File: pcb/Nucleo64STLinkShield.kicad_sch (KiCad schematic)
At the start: 6 parts, among them J1 SWD, J2 Debug, J3 UART, J4 USB Power, J5 Nucleo-64 ST-Link Selector

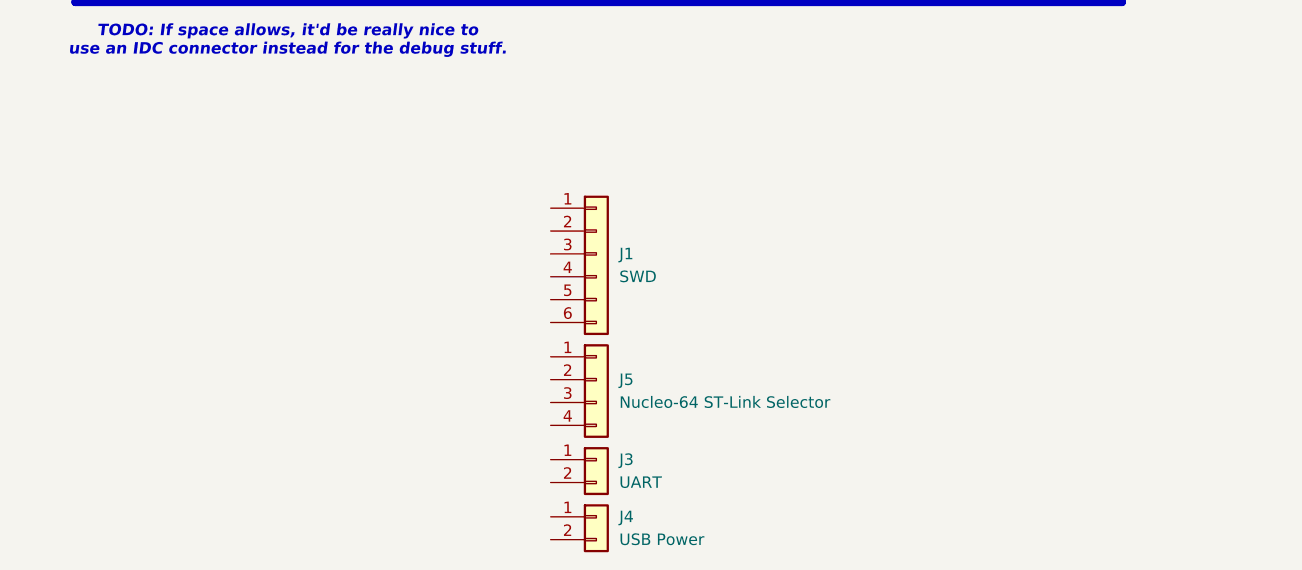
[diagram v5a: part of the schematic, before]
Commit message: Added nets for the pin sockets.
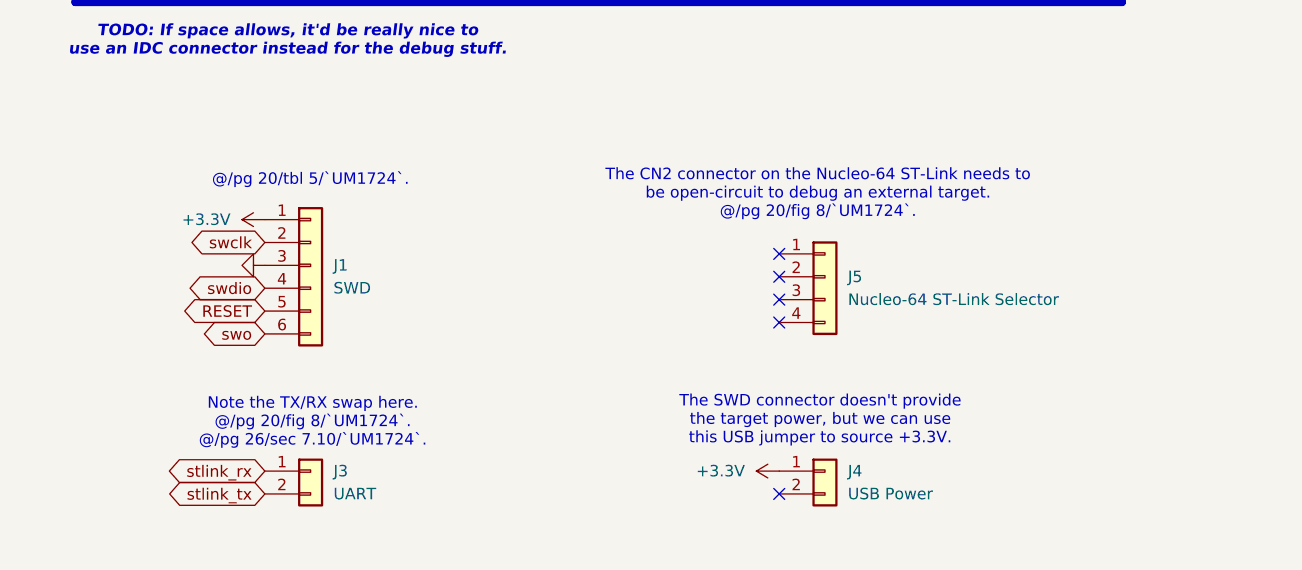
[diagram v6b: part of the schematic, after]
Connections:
- net +3.3V: now also J1.1 (Pin_1), J4.1 (Pin_1)
- net GND: now also J1.3 (Pin_3)
- net RESET: now also J1.5 (Pin_5)
- net stlink_rx: now also J3.1 (Pin_1)
- net stlink_tx: now also J3.2 (Pin_2)
- net swclk: now also J1.2 (Pin_2)
- net swdio: now also J1.4 (Pin_4)
- net swo: now also J1.6 (Pin_6)
- no-connect marks 0 -> 5
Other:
- note added: "@/pg 20/tbl 5/`UM1724`."
- note added: "Note the TX/RX swap here. @/pg 20/fig 8/`UM1724`. @/pg 26/sec 7.10/`UM1724`."
- note added: "The CN2 connector on the Nucleo-64 ST-Link needs to be open-circuit to debug an external target. @/pg 20/fig 8/`UM1724`."
- note added: "The SWD connector doesn't provide the target power, but we can use this USB jumper to source +3.3V."
- moved on the sheet: J1, J3, J4, J5

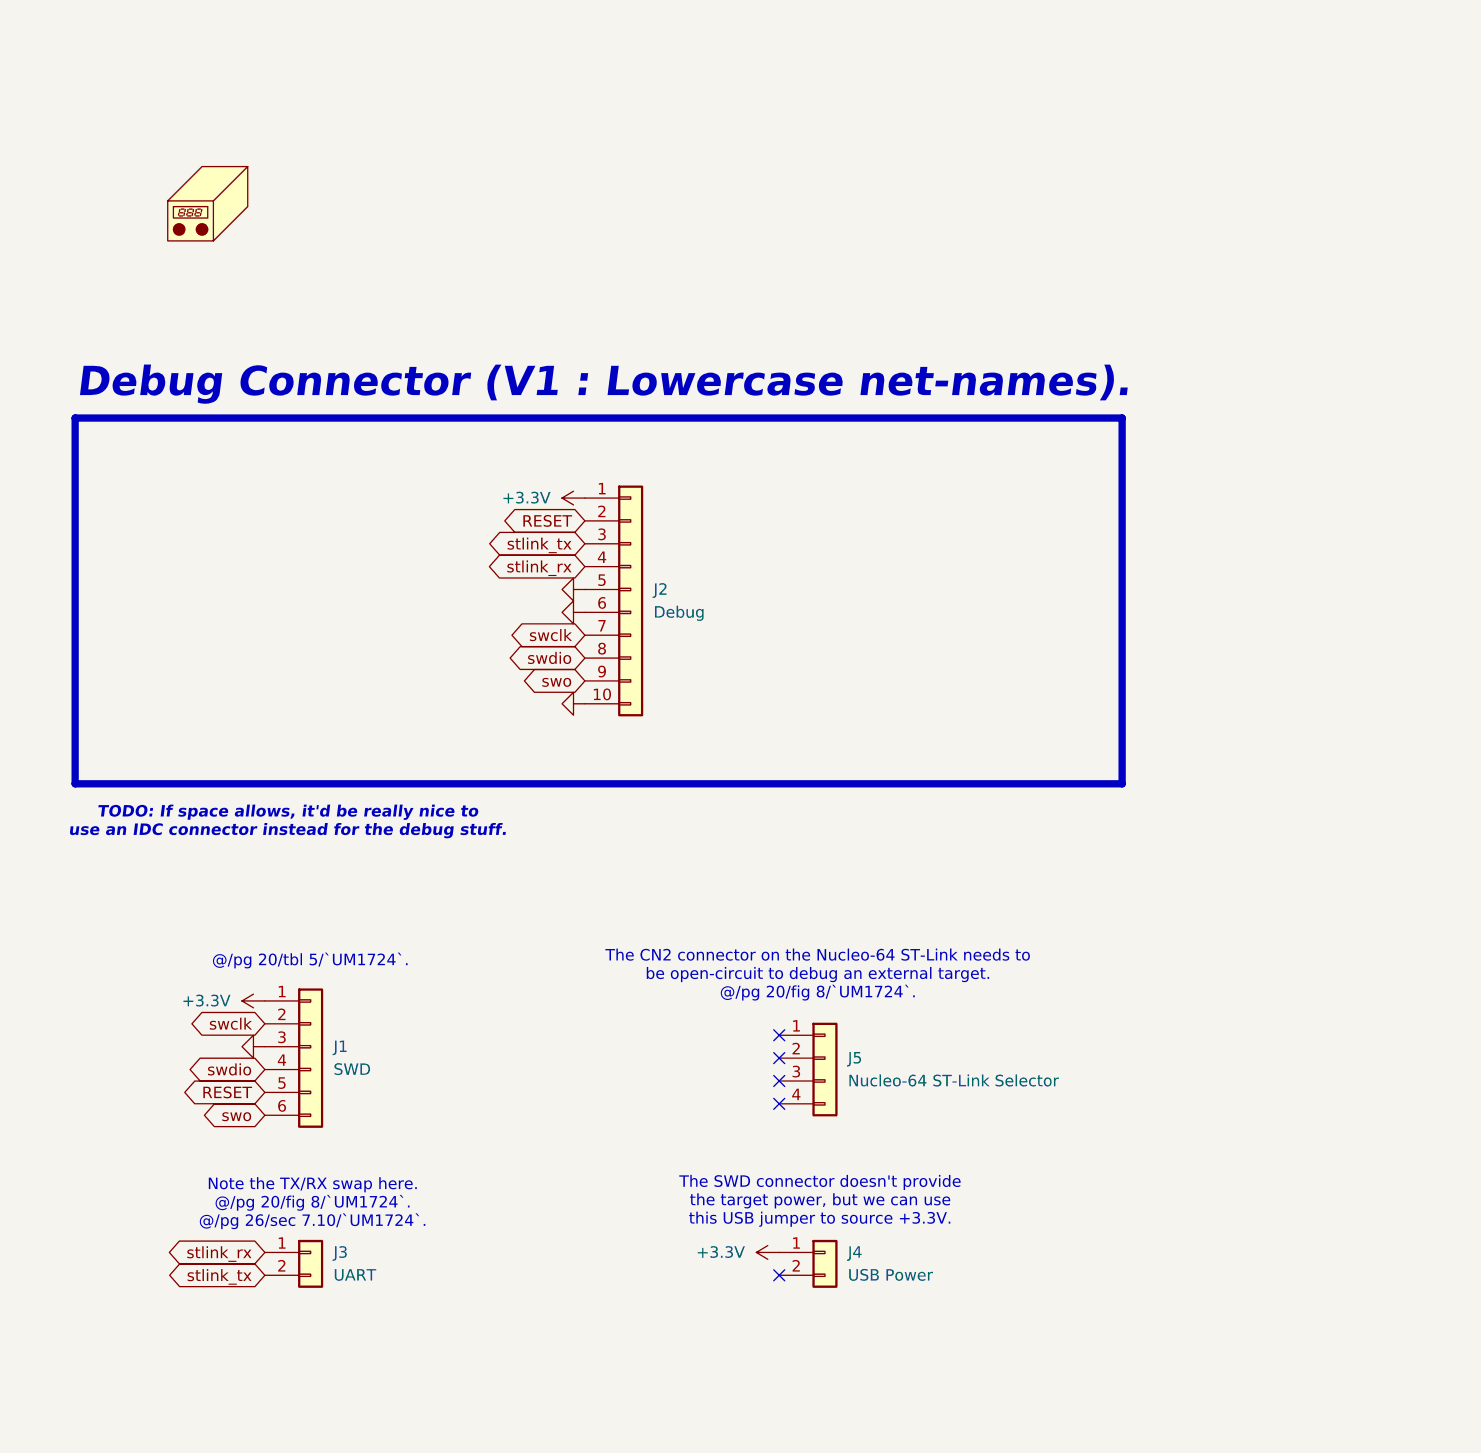
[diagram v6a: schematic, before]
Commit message: Added supporting components.
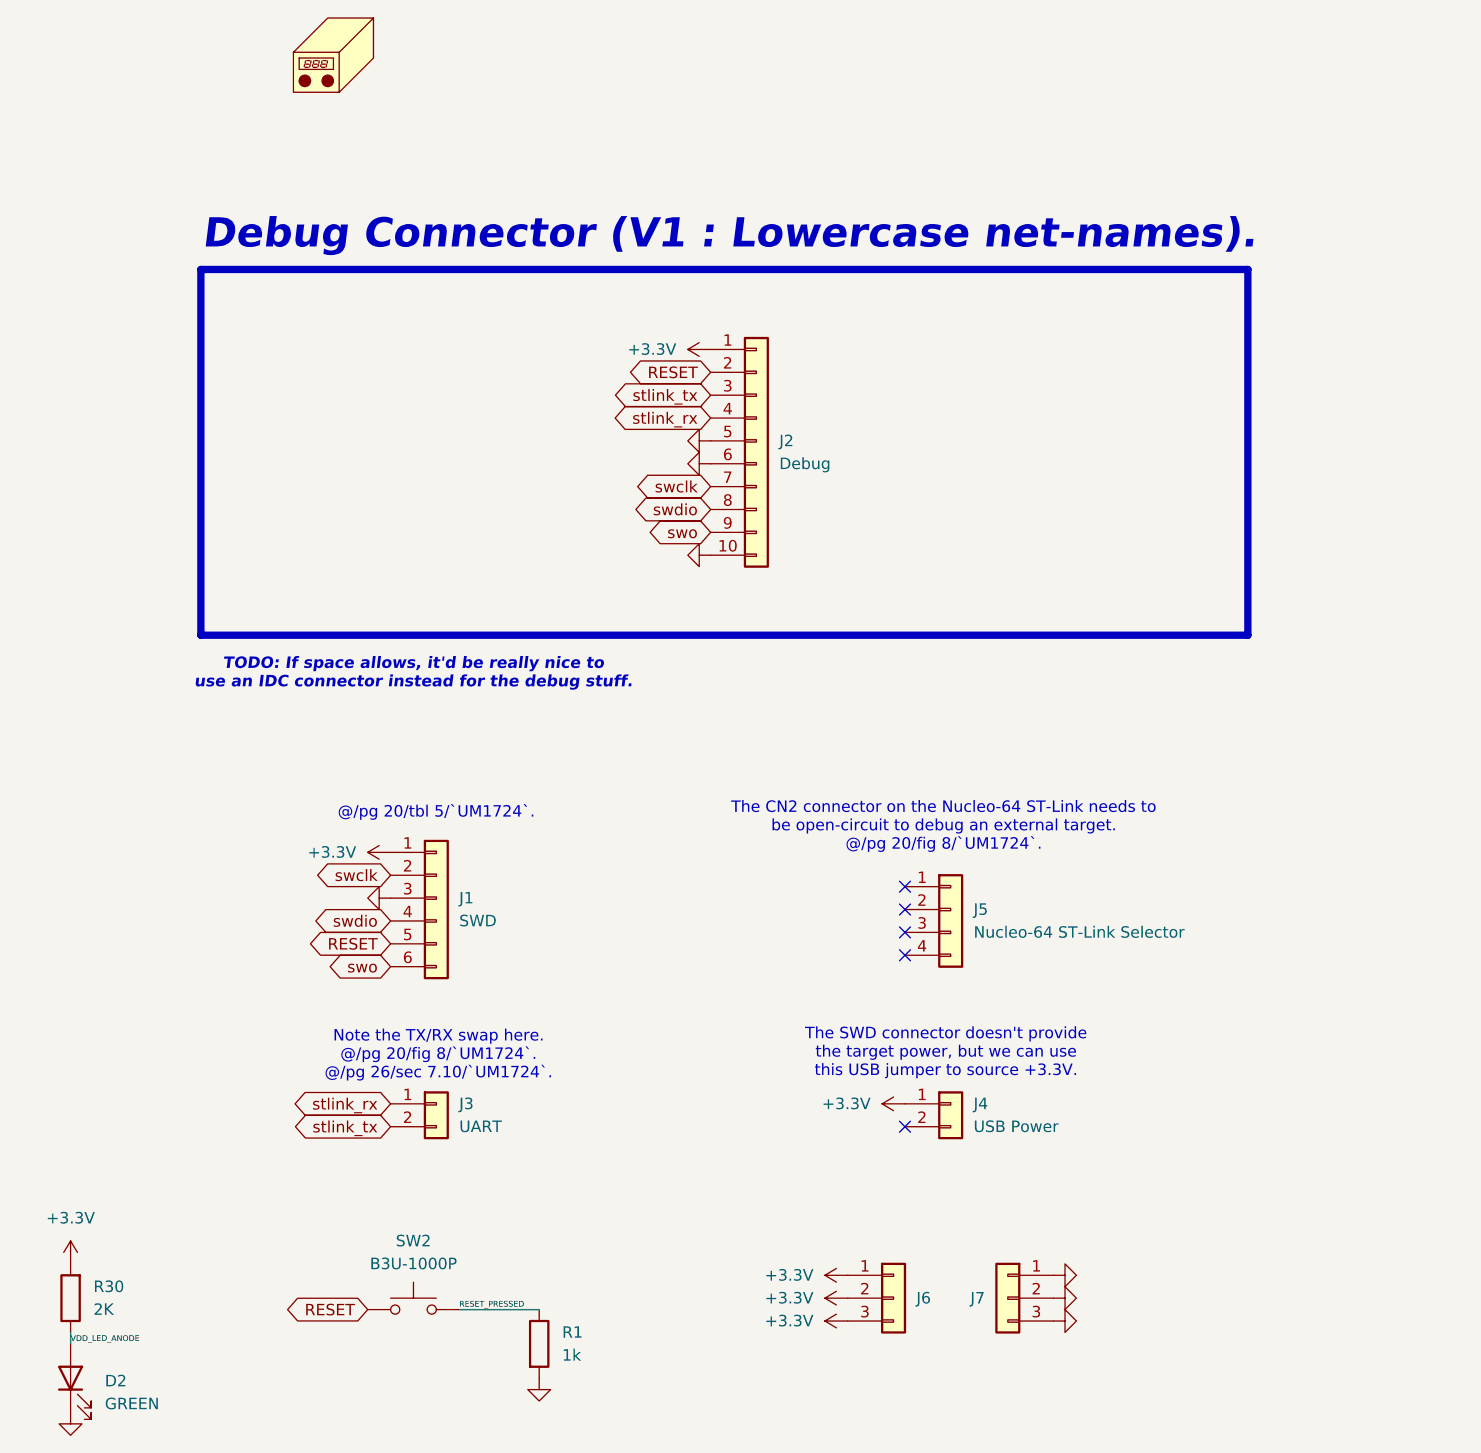
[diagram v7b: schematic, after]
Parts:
- added D2: GREEN, LED_SMD:LED_1206_3216Metric_Pad1.42x1.75mm_HandSolder, symbol Device:LED
- added J6, J7: Conn_01x06, Connector_PinHeader_2.54mm:PinHeader_1x03_P2.54mm_Vertical, symbol Connector_Generic:Conn_01x03
- added R1: 1k, Resistor_SMD:R_1206_3216Metric_Pad1.30x1.75mm_HandSolder, symbol Device:R
- added R30: 2K, Resistor_SMD:R_1206_3216Metric_Pad1.30x1.75mm_HandSolder, symbol Device:R
- added SW2: B3U-1000P, Button_Switch_SMD:SW_SPST_B3U-1000P, symbol Switch:SW_Push
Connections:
- net +3.3V: now also J6.1 (Pin_1), J6.2 (Pin_2), J6.3 (Pin_3), R30.2
- net GND: now also D2.1 (K), J7.1 (Pin_1), J7.2 (Pin_2), J7.3 (Pin_3), R1.2
- net RESET: now also SW2.2
- new net RESET_PRESSED: R1.1, SW2.1
- new net VDD_LED_ANODE: D2.2 (A), R30.1
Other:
- moved on the sheet: J1, J2, J3, J4, J5

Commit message: Routed the ST-Link shield.
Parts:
- J6, J7: value Conn_01x06 -> Conn_01x03
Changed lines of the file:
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@@
+	)
+	(symbol
+		(lib_id "power:GND")
+		(at 119.38 127 270)
+		(unit 1)
+		(exclude_from_sim no)
+		(in_bom yes)
+		(on_board yes)
+		(dnp no)
+		(fields_autoplaced yes)
+		(property "Reference" "#PWR02"
+			(at 113.03 127 0)
+			(effects
+				(font
+					(size 1.27 1.27)
+				)
+				(hide yes)
+			)
+		)
+		(property "Value" "GND"
+			(at 115.57 127.0001 90)
+			(effects
+				(font
+					(size 1.27 1.27)
+				)
+				(justify right)
+				(hide yes)
+			)
+		)
+		(property "Footprint" ""
+			(at 119.38 127 0)
+			(effects
+				(font
+					(size 1.27 1.27)
+				)
+				(hide yes)
+			)
+		)
+		(property "Datasheet" ""
+			(at 119.38 127 0)
+			(effects
+				(font
+					(size 1.27 1.27)
+				)
+				(hide yes)
+			)
+		)
+		(property "Description" "Power symbol creates a global label with name \"GND\" , ground"
+			(at 119.38 127 0)
+			(effects
+				(font
+					(size 1.27 1.27)
+				)
+				(hide yes)
+			)
+		)
+		(pin "1"
+		)
+		(instances
+			(project "Nucleo64STLinkShield"
+				(path "/dc931235-6a3d-461b-9fb0-f5879d72cf99"
+					(reference "#PWR02")
+					(unit 1)
+				)
+			)
+		)
 	)
 	(symbol
@@
 	)
 	(symbol
+		(lib_id "Connector_Generic:Conn_01x06")
+		(at 124.46 127 0)
+		(unit 1)
+		(exclude_from_sim no)
+		(in_bom yes)
+		(on_board yes)
+		(dnp no)
+		(property "Reference" "J1"
+			(at 127 127 0)
+			(effects
+				(font
+					(size 1.27 1.27)
+				)
+				(justify left)
+			)
+		)
+		(property "Value" "SWD"
+			(at 127 129.5399 0)
+			(effects
+				(font
+					(size 1.27 1.27)
+				)
+				(justify left)
+			)
+		)
+		(property "Footprint" "Connector_PinSocket_2.54mm:PinSocket_1x06_P2.54mm_Vertical"
+			(at 124.46 127 0)
+			(effects
+				(font
+					(size 1.27 1.27)
+				)
+				(hide yes)
+			)
+		)
+		(property "Datasheet" "~"
+			(at 124.46 127 0)
+			(effects
+				(font
+					(size 1.27 1.27)
+				)
+				(hide yes)
+			)
+		)
+		(property "Description" "Generic connector, single row, 01x06, script generated (kicad-library-utils/schlib/autogen/connector/)"
+			(at 124.46 127 0)
+			(effects
+				(font
+					(size 1.27 1.27)
+				)
+				(hide yes)
+			)
+		)
+		(pin "2"
+		)
+		(pin "1"
+		)
+		(pin "3"
+		)
+		(pin "5"
+		)
+		(pin "4"
+		)
+		(pin "6"
+		)
+		(instances
+			(project "Nucleo64STLinkShield"
+				(path "/dc931235-6a3d-461b-9fb0-f5879d72cf99"
+					(reference "J1")
+					(unit 1)
+				)
+			)
+		)
+	)
+	(symbol
 		(lib_id "power:GND")
 		(at 193.04 168.91 90)
@@
 	)
 	(symbol
-		(lib_id "power:GND")
-		(at 119.38 127 270)
-		(unit 1)
-		(exclude_from_sim no)
-		(in_bom yes)
-		(on_board yes)
-		(dnp no)
-		(fields_autoplaced yes)
-		(property "Reference" "#PWR02"
-			(at 113.03 127 0)
-			(effects
-				(font
-					(size 1.27 1.27)
-				)
-				(hide yes)
-			)
-		)
-		(property "Value" "GND"
-			(at 115.57 127.0001 90)
-			(effects
-				(font
-					(size 1.27 1.27)
-				)
-				(justify right)
-				(hide yes)
-			)
-		)
-		(property "Footprint" ""
-			(at 119.38 127 0)
-			(effects
-				(font
-					(size 1.27 1.27)
-				)
-				(hide yes)
-			)
-		)
-		(property "Datasheet" ""
-			(at 119.38 127 0)
-			(effects
-				(font
-					(size 1.27 1.27)
-				)
-				(hide yes)
-			)
-		)
-		(property "Description" "Power symbol creates a global label with name \"GND\" , ground"
-			(at 119.38 127 0)
-			(effects
-				(font
-					(size 1.27 1.27)
-				)
-				(hide yes)
-			)
-		)
-		(pin "1"
-		)
-		(instances
-			(project "Nucleo64STLinkShield"
-				(path "/dc931235-6a3d-461b-9fb0-f5879d72cf99"
-					(reference "#PWR02")
-					(unit 1)
-				)
-			)
-		)
-	)
-	(symbol
 		(lib_id "power:+3.3V")
 		(at 119.38 121.92 90)
@@
 				(path "/dc931235-6a3d-461b-9fb0-f5879d72cf99"
 					(reference "#PWR01")
-					(unit 1)
-				)
-			)
-		)
-	)
-	(symbol
-		(lib_id "Connector_Generic:Conn_01x06")
-		(at 124.46 127 0)
-		(unit 1)
-		(exclude_from_sim no)
-		(in_bom yes)
-		(on_board yes)
-		(dnp no)
-		(fields_autoplaced yes)
-		(property "Reference" "J1"
-			(at 127 126.9999 0)
-			(effects
-				(font
-					(size 1.27 1.27)
-				)
-				(justify left)
-			)
-		)
-		(property "Value" "SWD"
-			(at 127 129.5399 0)
-			(effects
-				(font
-					(size 1.27 1.27)
-				)
-				(justify left)
-			)
-		)
-		(property "Footprint" "Connector_PinSocket_2.54mm:PinSocket_1x06_P2.54mm_Vertical"
-			(at 124.46 127 0)
-			(effects
-				(font
-					(size 1.27 1.27)
-				)
-				(hide yes)
-			)
-		)
-		(property "Datasheet" "~"
-			(at 124.46 127 0)
-			(effects
-				(font
-					(size 1.27 1.27)
-				)
-				(hide yes)
-			)
-		)
-		(property "Description" "Generic connector, single row, 01x06, script generated (kicad-library-utils/schlib/autogen/connector/)"
-			(at 124.46 127 0)
-			(effects
-				(font
-					(size 1.27 1.27)
-				)
-				(hide yes)
-			)
-		)
-		(pin "6"
-		)
-		(pin "5"
-		)
-		(pin "2"
-		)
-		(pin "3"
-		)
-		(pin "4"
-		)
-		(pin "1"
-		)
-		(instances
-			(project ""
-				(path "/dc931235-6a3d-461b-9fb0-f5879d72cf99"
-					(reference "J1")
 					(unit 1)
 				)
@@
 			)
 		)
-		(property "Value" "Conn_01x06"
+		(property "Value" "Conn_01x03"
 			(at 185.42 173.9899 0)
 			(effects
@@
 			)
 		)
-		(property "Value" "Conn_01x06"
+		(property "Value" "Conn_01x03"
 			(at 177.8 173.9899 0)
 			(effects
